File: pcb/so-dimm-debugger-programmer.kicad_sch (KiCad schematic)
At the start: 21 parts, among them J1 1612618-4, J2 Conn_01x06_Male, J3 Conn_01x06_Male, J4 Conn_01x04_Male, J5 Conn_01x04_Male, J8 Conn_02x16_Odd_Even, U1 AP2112K-3.3

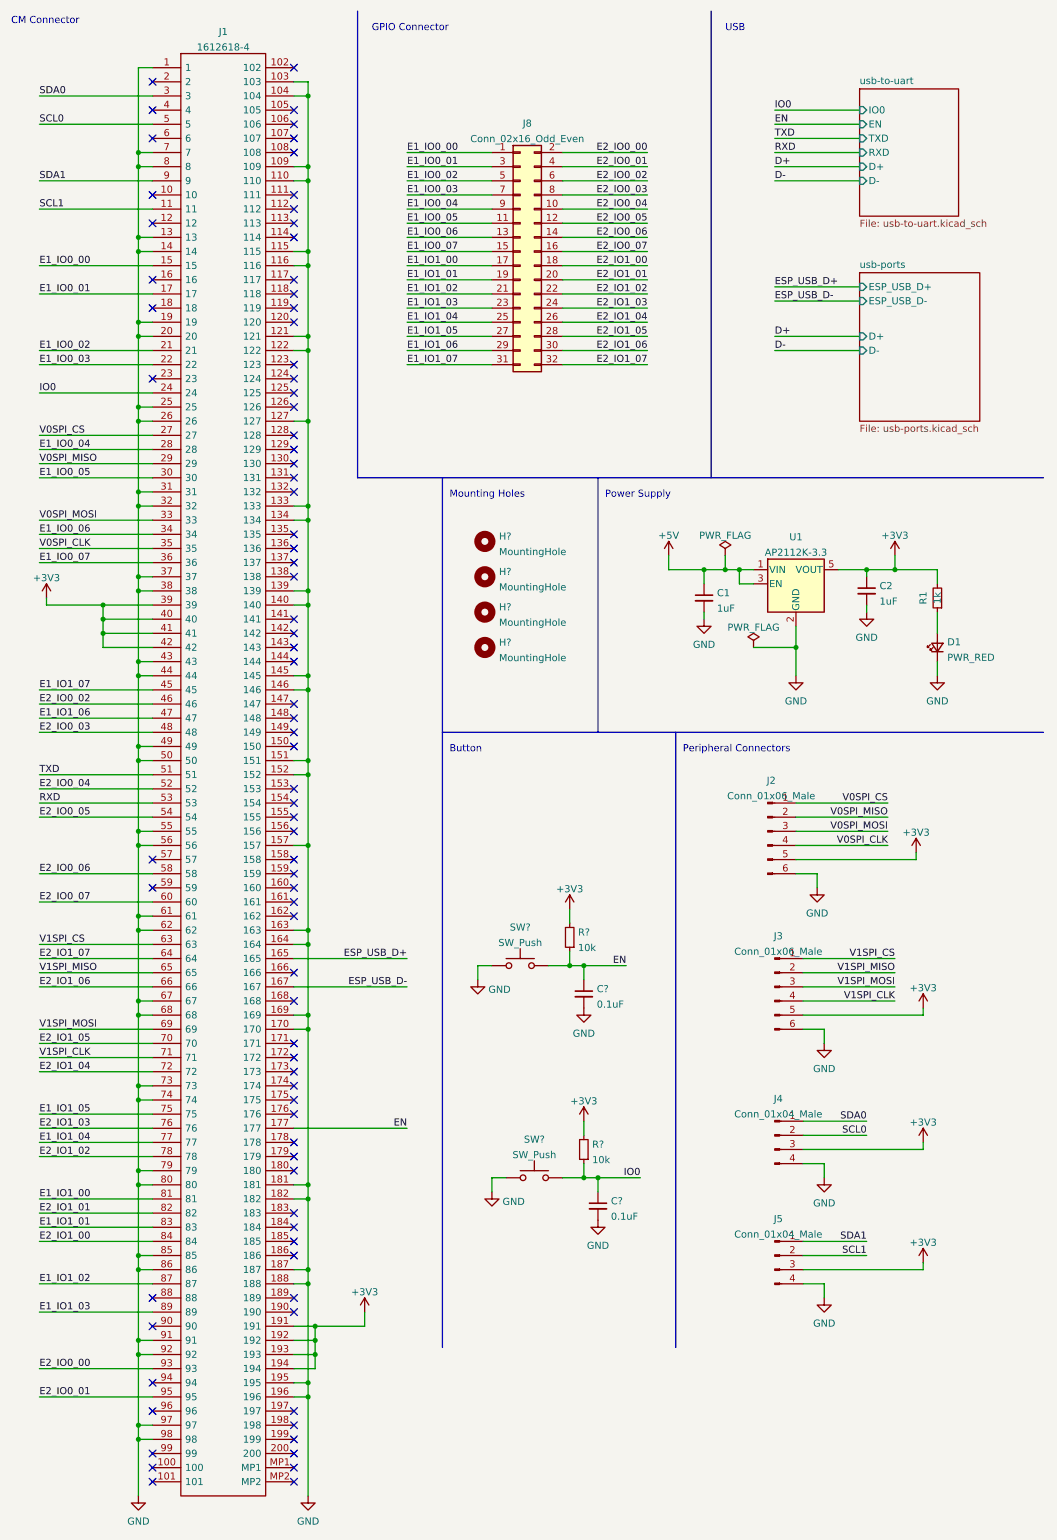
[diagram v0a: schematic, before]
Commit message: Added first version of the pcb layout
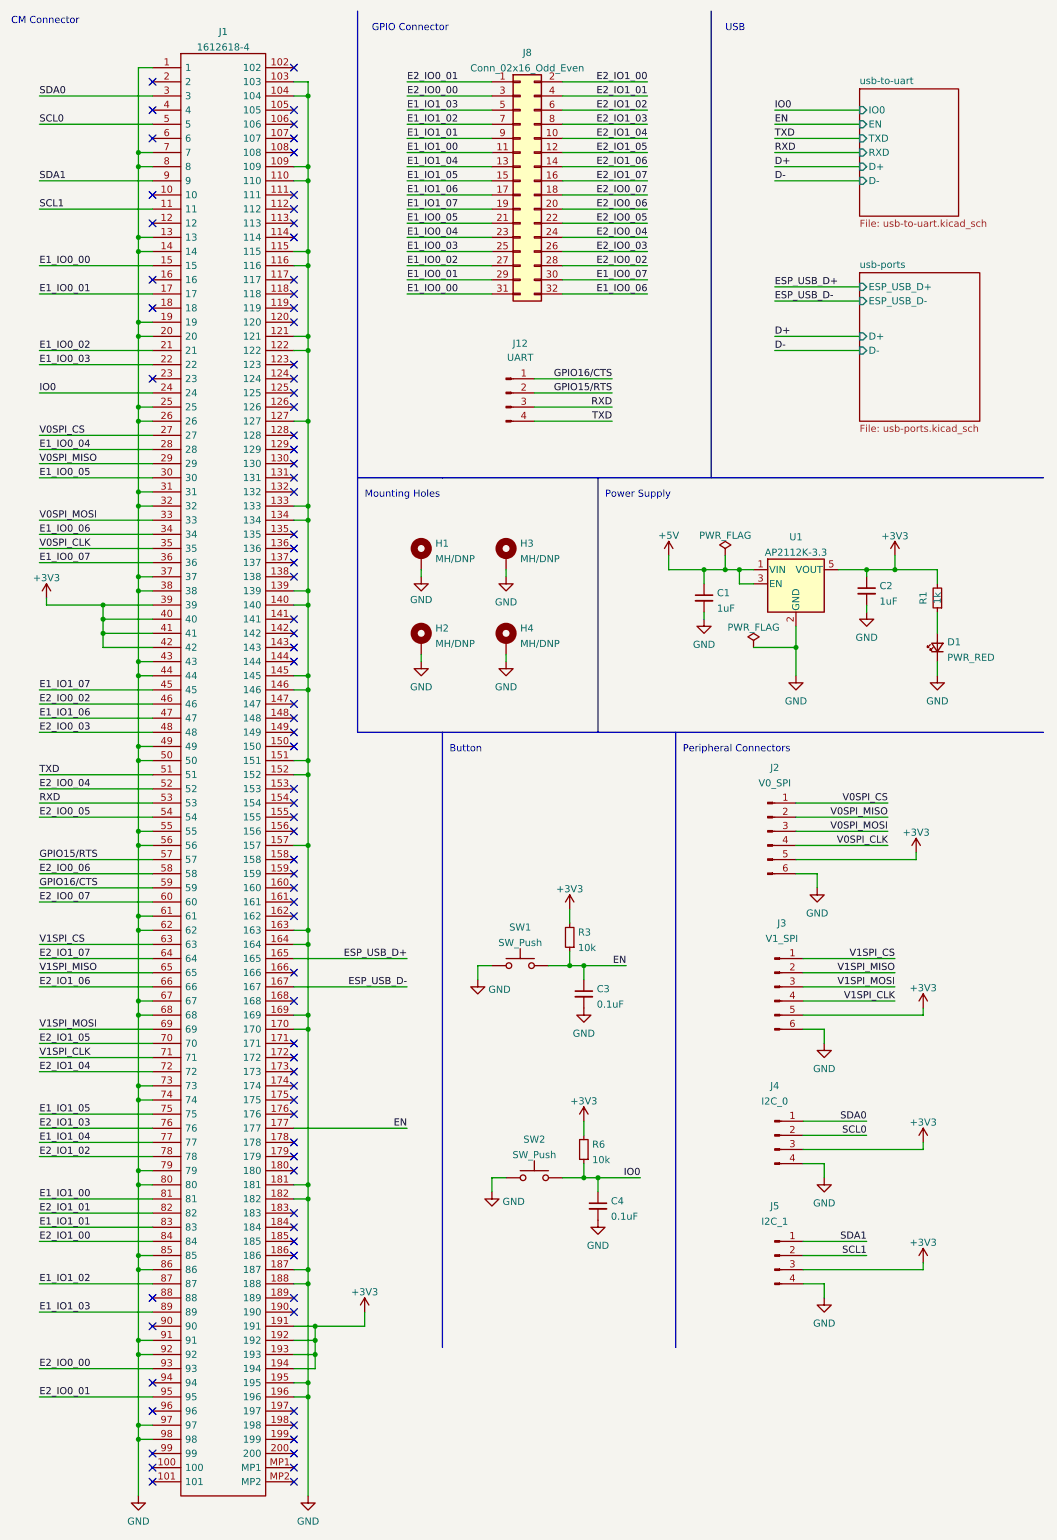
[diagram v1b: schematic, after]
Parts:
- removed H? (x4): MountingHole, symbol Mechanical:MountingHole
- added H1, H2, H3, H4: MH/DNP, MountingHole:MountingHole_2.5mm_Pad_Via, symbol Mechanical:MountingHole_Pad
- added J12: UART, Connector_PinHeader_2.54mm:PinHeader_1x04_P2.54mm_Vertical, symbol Connector:Conn_01x04_Male
- J2: value Conn_01x06_Male -> V0_SPI
- J3: value Conn_01x06_Male -> V1_SPI
- J4: value Conn_01x04_Male -> I2C_0
- J5: value Conn_01x04_Male -> I2C_1
- J8: footprint Connector_PinSocket_2.54mm:PinSocket_2x16_P2.54mm_Vertical -> Connector_PinHeader_2.54mm:PinHeader_2x16_P2.54mm_Vertical
- SW1, SW2: renamed from SW?; footprint (none) -> SKRKAEE020:SKRKAEE020
- gave numbers to parts that had none: 4
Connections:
- net E1_IO0_00: now also J8.31 (Pin_31); no longer J8.1 (Pin_1)
- net E1_IO0_01: now also J8.29 (Pin_29); no longer J8.3 (Pin_3)
- net E1_IO0_02: now also J8.27 (Pin_27); no longer J8.5 (Pin_5)
- net E1_IO0_03: now also J8.25 (Pin_25); no longer J8.7 (Pin_7)
- net E1_IO0_04: now also J8.23 (Pin_23); no longer J8.9 (Pin_9)
- net E1_IO0_05: now also J8.21 (Pin_21); no longer J8.11 (Pin_11)
- net E1_IO0_06: now also J8.32 (Pin_32); no longer J8.13 (Pin_13)
- net E1_IO0_07: now also J8.30 (Pin_30); no longer J8.15 (Pin_15)
- net E1_IO1_00: now also J8.11 (Pin_11); no longer J8.17 (Pin_17)
- net E1_IO1_01: now also J8.9 (Pin_9); no longer J8.19 (Pin_19)
- net E1_IO1_02: now also J8.7 (Pin_7); no longer J8.21 (Pin_21)
- net E1_IO1_03: now also J8.5 (Pin_5); no longer J8.23 (Pin_23)
- net E1_IO1_04: now also J8.13 (Pin_13); no longer J8.25 (Pin_25)
- net E1_IO1_05: now also J8.15 (Pin_15); no longer J8.27 (Pin_27)
- net E1_IO1_06: now also J8.17 (Pin_17); no longer J8.29 (Pin_29)
- net E1_IO1_07: now also J8.19 (Pin_19); no longer J8.31 (Pin_31)
- net E2_IO0_00: now also J8.3 (Pin_3); no longer J8.2 (Pin_2)
- net E2_IO0_01: now also J8.1 (Pin_1); no longer J8.4 (Pin_4)
- net E2_IO0_02: now also J8.28 (Pin_28); no longer J8.6 (Pin_6)
- net E2_IO0_03: now also J8.26 (Pin_26); no longer J8.8 (Pin_8)
- net E2_IO0_04: now also J8.24 (Pin_24); no longer J8.10 (Pin_10)
- net E2_IO0_05: now also J8.22 (Pin_22); no longer J8.12 (Pin_12)
- net E2_IO0_06: now also J8.20 (Pin_20); no longer J8.14 (Pin_14)
- net E2_IO0_07: now also J8.18 (Pin_18); no longer J8.16 (Pin_16)
- net E2_IO1_00: now also J8.2 (Pin_2); no longer J8.18 (Pin_18)
- net E2_IO1_01: now also J8.4 (Pin_4); no longer J8.20 (Pin_20)
- net E2_IO1_02: now also J8.6 (Pin_6); no longer J8.22 (Pin_22)
- net E2_IO1_03: now also J8.8 (Pin_8); no longer J8.24 (Pin_24)
- net E2_IO1_04: now also J8.10 (Pin_10); no longer J8.26 (Pin_26)
- net E2_IO1_05: now also J8.12 (Pin_12); no longer J8.28 (Pin_28)
- net E2_IO1_06: now also J8.14 (Pin_14); no longer J8.30 (Pin_30)
- net E2_IO1_07: now also J8.16 (Pin_16); no longer J8.32 (Pin_32)
- net GND: now also H1.1, H2.1, H3.1, H4.1
- net RXD: now also J12.3 (Pin_3)
- net TXD: now also J12.4 (Pin_4)
- net GPIO15/RTS: now reaches J1.57
- net GPIO15/RTS: now also J12.2 (Pin_2)
- net GPIO16/CTS: now reaches J1.59
- net GPIO16/CTS: now also J12.1 (Pin_1)
- no-connect marks 83 -> 81
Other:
- moved on the sheet: J8

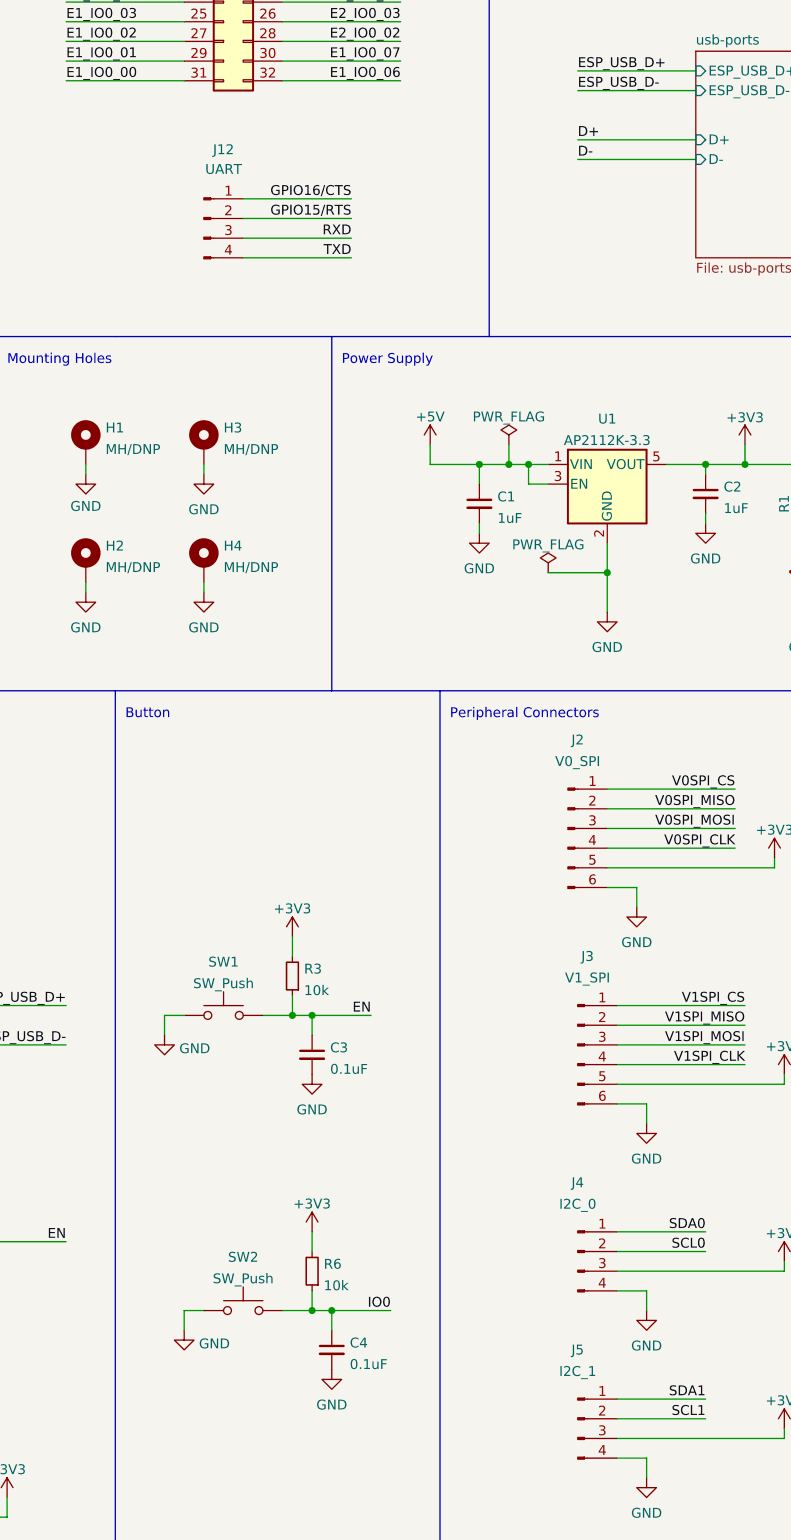
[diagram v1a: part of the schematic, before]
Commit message: Try to fix all ERC and DRC Issues and Warning + changed violation config
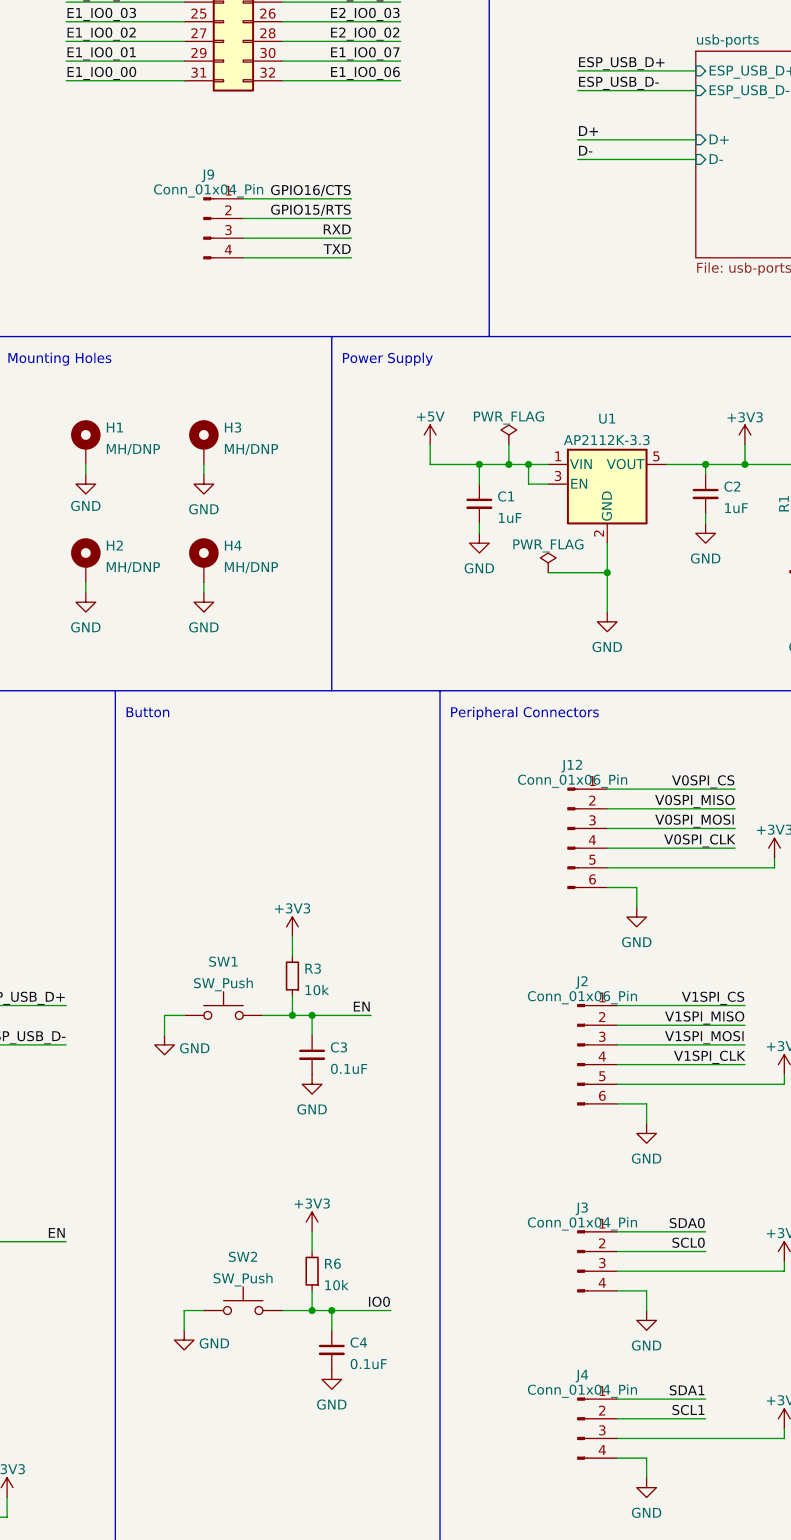
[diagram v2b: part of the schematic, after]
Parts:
- removed J12: UART, Connector_PinHeader_2.54mm:PinHeader_1x04_P2.54mm_Vertical, symbol Connector:Conn_01x04_Male
- removed J2: V0_SPI, Connector_PinHeader_2.54mm:PinHeader_1x06_P2.54mm_Vertical, symbol Connector:Conn_01x06_Male
- removed J3: V1_SPI, Connector_PinHeader_2.54mm:PinHeader_1x06_P2.54mm_Vertical, symbol Connector:Conn_01x06_Male
- removed J4: I2C_0, Connector_PinHeader_2.54mm:PinHeader_1x04_P2.54mm_Vertical, symbol Connector:Conn_01x04_Male
- removed J5: I2C_1, Connector_PinHeader_2.54mm:PinHeader_1x04_P2.54mm_Vertical, symbol Connector:Conn_01x04_Male
- added J12, J2: Conn_01x06_Pin, Connector_PinHeader_2.54mm:PinHeader_1x06_P2.54mm_Vertical, symbol Connector:Conn_01x06_Pin
- added J3, J4, J9: Conn_01x04_Pin, Connector_PinHeader_2.54mm:PinHeader_1x04_P2.54mm_Vertical, symbol Connector:Conn_01x04_Pin
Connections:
- net +3V3: now also J12.5 (Pin_5), J2.5 (Pin_5), J3.3 (Pin_3), J4.3 (Pin_3)
- net GND: now also J12.6 (Pin_6), J2.6 (Pin_6), J3.4 (Pin_4), J4.4 (Pin_4)
- net GPIO15/RTS: now also J9.2 (Pin_2)
- net GPIO16/CTS: now also J9.1 (Pin_1)
- net RXD: now also J9.3 (Pin_3)
- net SCL0: now also J3.2 (Pin_2)
- net SCL1: now also J4.2 (Pin_2)
- net SDA0: now also J3.1 (Pin_1)
- net SDA1: now also J4.1 (Pin_1)
- net TXD: now also J9.4 (Pin_4)
- net V0SPI_CLK: now also J12.4 (Pin_4)
- net V0SPI_CS: now also J12.1 (Pin_1)
- net V0SPI_MISO: now also J12.2 (Pin_2)
- net V0SPI_MOSI: now also J12.3 (Pin_3)
- net V1SPI_CLK: now also J2.4 (Pin_4)
- net V1SPI_CS: now also J2.1 (Pin_1)
- net V1SPI_MISO: now also J2.2 (Pin_2)
- net V1SPI_MOSI: now also J2.3 (Pin_3)
